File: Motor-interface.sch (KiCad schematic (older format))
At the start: 40 parts, among them J101 0, J102 0, K101 RELAY_2RT, P101 TE-23pins connector, P102 PSU_ISO, P103 Halls, P104 LineContactor, P105 ReverseContactor, P106 FanContactor, P107 Battery+, P108 MC_USB, P109 MC_CAN, Q101 Q_NPN_BCE, U101 AP1117D50, U102 AP1117D33, U103 TLP2361, U104 TLP2361, U105 TLP2361, U106 TLP2361, U107 TLP2361, U108 TLP2361, U109 Teensy_3.2, U110 TLP2361

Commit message: PBC layout
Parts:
- U109: footprint Housings_SSOP:TSSOP-32_6.1x11mm_Pitch0.65mm -> electric_car_lib:Teensy3.2_inv
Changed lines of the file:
@@
 F 0 "U109" H 8000 1750 39  0000 C CNN
 F 1 "Teensy_3.2" H 8000 2450 39  0000 C CNN
-F 2 "Housings_SSOP:TSSOP-32_6.1x11mm_Pitch0.65mm" H 7700 1450 39  0001 C CNN
+F 2 "electric_car_lib:Teensy3.2_inv" H 7700 1450 39  0001 C CNN
 F 3 "" H 7700 1450 39  0000 C CNN
 	1    8000 1900
@@
 	8350 5000 8350 5050
 Wire Wire Line
-	8350 5450 8350 5550
+	8350 5450 8350 5500
+Wire Wire Line
+	8350 5500 8350 5550
 Wire Wire Line
 	8600 5400 8600 5500
@@
 	8600 5000 8600 5100
 Wire Wire Line
-	7600 5000 8600 5000
+	7600 5000 8350 5000
+Wire Wire Line
+	8350 5000 8600 5000
 Connection ~ 8350 5000
 Wire Wire Line
@@
 Hall_Power
 Wire Wire Line
-	4250 3700 4550 3700
+	4250 3700 4450 3700
+Wire Wire Line
+	4450 3700 4550 3700
 Wire Wire Line
 	4850 3700 4950 3700
@@
 	4950 4700 4850 4700
 Wire Wire Line
-	4450 3700 4450 4700
+	4450 3700 4450 4200
+Wire Wire Line
+	4450 4200 4450 4700
 Wire Wire Line
 	4450 4700 4550 4700

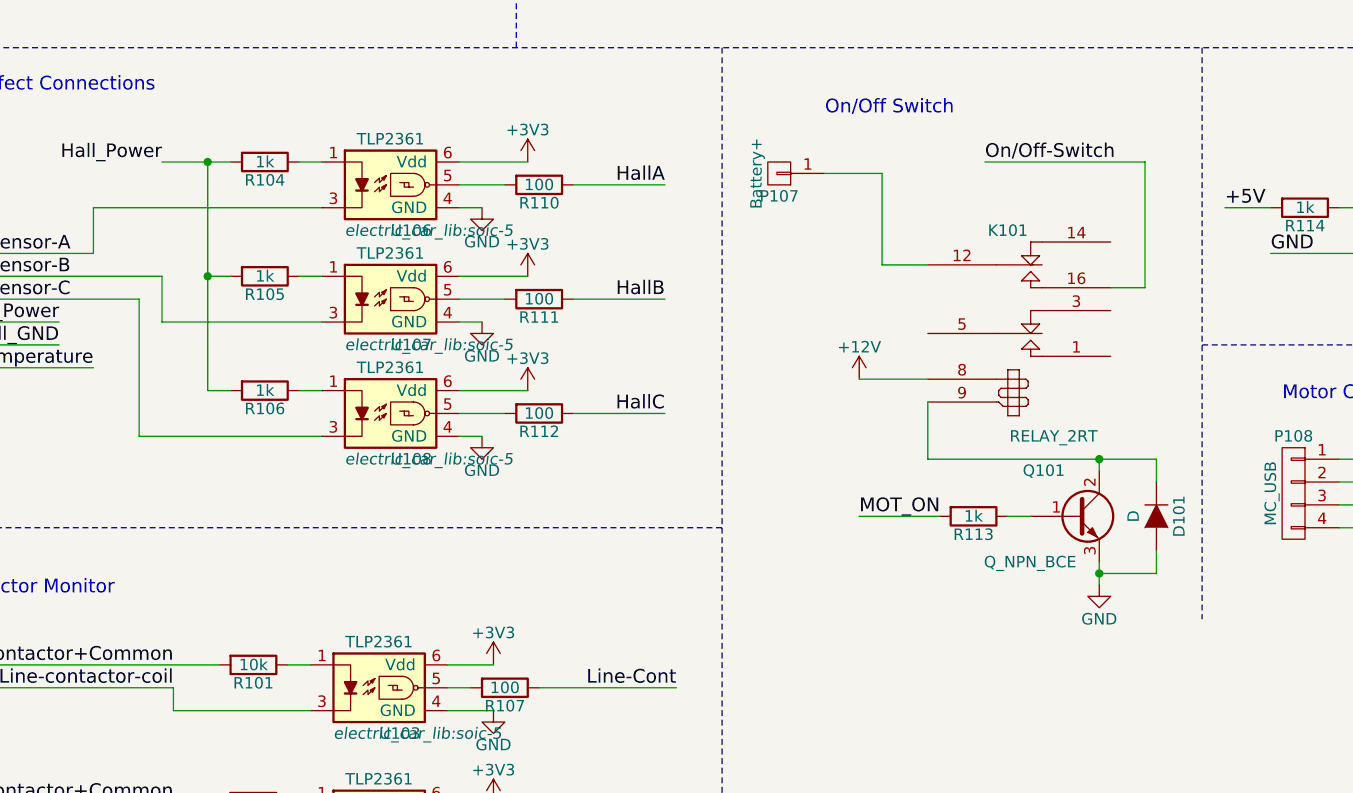
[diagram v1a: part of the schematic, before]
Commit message: changed optos, removed relay, needs ssr
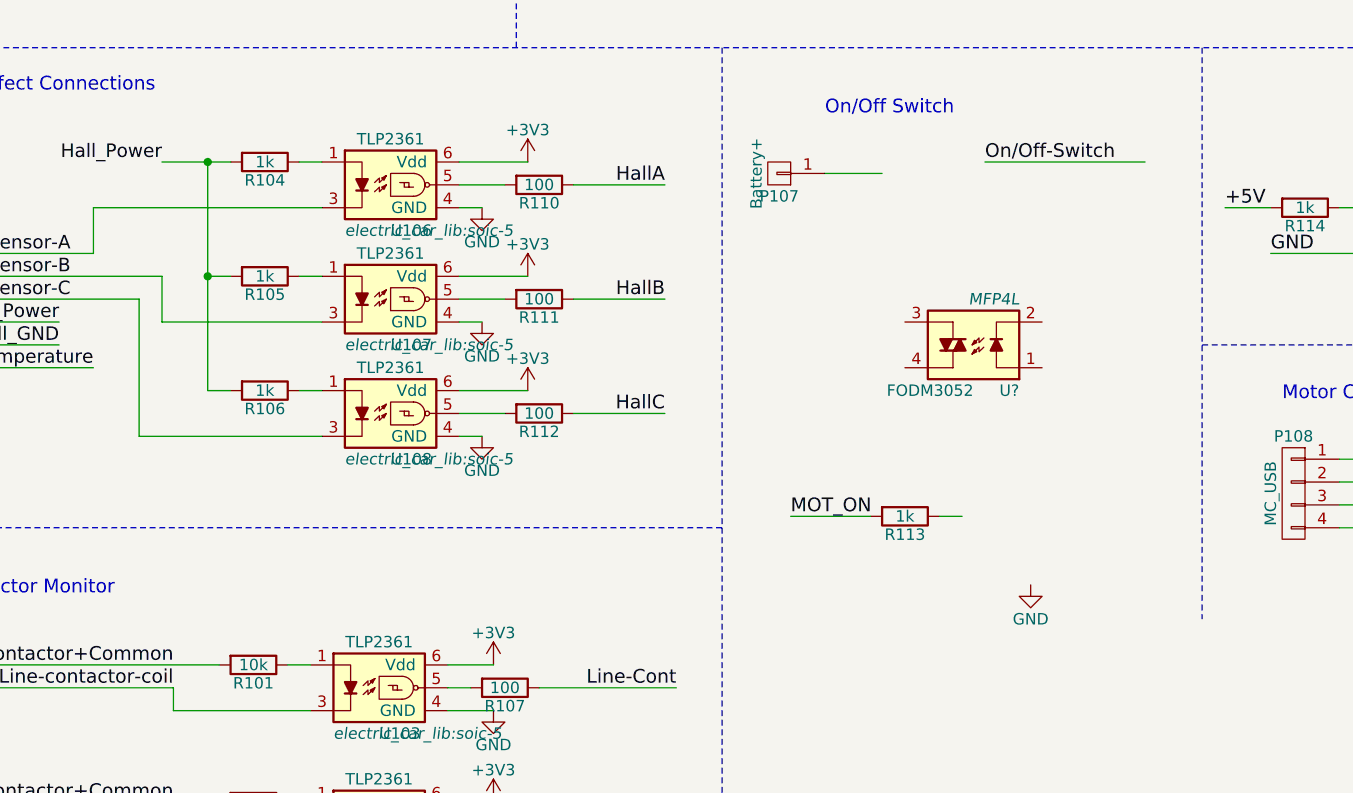
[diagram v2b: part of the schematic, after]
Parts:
- removed D101: D, Diodes_SMD:DO-214AB_Handsoldering, symbol D
- removed K101: RELAY_2RT, Relays_ThroughHole:Relay_SANYOU_SRD_Series_Form_C, symbol RELAY_2RT
- removed Q101: Q_NPN_BCE, TO_SOT_Packages_SMD:SOT-23, symbol Q_NPN_BCE
- added U?: FODM3052, MFP4L, symbol FODM3052
- U101, U102: footprint TO_SOT_Packages_SMD:TO-252-2Lead -> TO_SOT_Packages_SMD:SOT-223
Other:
- moved on the sheet: R113
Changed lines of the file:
@@
 MOSI
-$Comp
-L RELAY_2RT K101
-U 1 1 57FCBA72
-P 8000 4400
-F 0 "K101" H 7950 4800 50  0000 C CNN
-F 1 "RELAY_2RT" H 8150 3900 50  0000 C CNN
-F 2 "Relays_ThroughHole:Relay_SANYOU_SRD_Series_Form_C" H 8000 4400 50  0001 C CNN
-F 3 "" H 8000 4400 50  0000 C CNN
-	1    8000 4400
-	1    0    0    -1
-$EndComp
-$Comp
-L Q_NPN_BCE Q101
-U 1 1 57FCBE60
-P 8250 5250
-F 0 "Q101" H 8200 5450 50  0000 R CNN
-F 1 "Q_NPN_BCE" H 8250 5050 50  0000 R CNN
-F 2 "TO_SOT_Packages_SMD:SOT-23" H 8450 5350 50  0001 C CNN
-F 3 "" H 8250 5250 50  0000 C CNN
-	1    8250 5250
-	1    0    0    -1
-$EndComp
-$Comp
-L +12V #PWR01
-U 1 1 57FCC08A
-P 7300 4650
-F 0 "#PWR01" H 7300 4500 50  0001 C CNN
-F 1 "+12V" H 7300 4790 50  0000 C CNN
-F 2 "" H 7300 4650 50  0000 C CNN
-F 3 "" H 7300 4650 50  0000 C CNN
-	1    7300 4650
-	-1   0    0    -1
-$EndComp
 $Comp
 L GND #PWR02
 U 1 1 57FCC1C9
-P 8350 5550
-F 0 "#PWR02" H 8350 5300 50  0001 C CNN
-F 1 "GND" H 8350 5400 50  0000 C CNN
-F 2 "" H 8350 5550 50  0000 C CNN
-F 3 "" H 8350 5550 50  0000 C CNN
-	1    8350 5550
-	1    0    0    -1
-$EndComp
-Text Label 7300 5250 0    60   ~ 0
+P 8050 5550
+F 0 "#PWR02" H 8050 5300 50  0001 C CNN
+F 1 "GND" H 8050 5400 50  0000 C CNN
+F 2 "" H 8050 5550 50  0000 C CNN
+F 3 "" H 8050 5550 50  0000 C CNN
+	1    8050 5550
+	1    0    0    -1
+$EndComp
+Text Label 7000 5250 0    60   ~ 0
 MOT_ON
 Text Label 9200 2200 2    60   ~ 0
@@
 L R R113
 U 1 1 581878E6
-P 7800 5250
-F 0 "R113" V 7880 5250 50  0000 C CNN
-F 1 "1k" V 7800 5250 50  0000 C CNN
-F 2 "Resistors_SMD:R_1206_HandSoldering" V 7730 5250 50  0001 C CNN
-F 3 "" H 7800 5250 50  0000 C CNN
-	1    7800 5250
+P 7500 5250
+F 0 "R113" V 7580 5250 50  0000 C CNN
+F 1 "1k" V 7500 5250 50  0000 C CNN
+F 2 "Resistors_SMD:R_1206_HandSoldering" V 7430 5250 50  0001 C CNN
+F 3 "" H 7500 5250 50  0000 C CNN
+	1    7500 5250
 	0    1    1    0
 $EndComp
@@
 	1    8850 1200
 	1    0    0    -1
-$EndComp
-$Comp
-L D D101
-U 1 1 582A630A
-P 8600 5250
-F 0 "D101" H 8600 5350 50  0000 C CNN
-F 1 "D" H 8600 5150 50  0000 C CNN
-F 2 "Diodes_SMD:DO-214AB_Handsoldering" H 8600 5250 50  0001 C CNN
-F 3 "" H 8600 5250 50  0000 C CNN
-	1    8600 5250
-	0    1    1    0
 $EndComp
 $Comp
@@
 Wire Wire Line
 	8700 2500 8900 2500
-Wire Wire Line
-	7300 4650 7600 4650
-Wire Wire Line
-	8550 4250 8400 4250
 Wire Notes Line
 	700  3200 10750 3200
@@
 	7150 3750 7400 3750
 Wire Wire Line
-	7400 3750 7400 4150
-Wire Wire Line
-	7400 4150 7600 4150
-Wire Wire Line
 	3200 5900 4500 5900
 Wire Wire Line
@@
 	3200 6600 4300 6600
 Wire Wire Line
-	7950 5250 8050 5250
-Wire Wire Line
-	7650 5250 7300 5250
+	7650 5250 7750 5250
+Wire Wire Line
+	7350 5250 7000 5250
 Wire Notes Line
 	2600 600  2600 7150
@@
 Wire Wire Line
 	8700 1200 8850 1200
-Wire Wire Line
-	8350 5000 8350 5050
-Wire Wire Line
-	8350 5450 8350 5500
-Wire Wire Line
-	8350 5500 8350 5550
-Wire Wire Line
-	8600 5400 8600 5500
-Wire Wire Line
-	8600 5500 8350 5500
-Connection ~ 8350 5500
-Wire Wire Line
-	8600 5000 8600 5100
-Wire Wire Line
-	7600 5000 8350 5000
-Wire Wire Line
-	8350 5000 8600 5000
-Connection ~ 8350 5000
 Wire Wire Line
 	6200 1500 7300 1500
@@
 Hall_Power
 Wire Wire Line
-	4250 3700 4450 3700
-Wire Wire Line
-	4450 3700 4550 3700
+	4250 3700 4550 3700
 Wire Wire Line
 	4850 3700 4950 3700
@@
 	4950 4700 4850 4700
 Wire Wire Line
-	4450 3700 4450 4200
-Wire Wire Line
-	4450 4200 4450 4700
+	4450 3700 4450 4700
 Wire Wire Line
 	4450 4700 4550 4700
@@
 F 0 "U102" H 2100 2050 50  0000 C CNN
 F 1 "AP1117D33" H 2000 2550 50  0000 C CNN
-F 2 "TO_SOT_Packages_SMD:TO-252-2Lead" H 2000 2300 50  0001 C CNN
+F 2 "TO_SOT_Packages_SMD:SOT-223" H 2000 2300 50  0001 C CNN
 F 3 "" H 2000 2300 50  0000 C CNN
 	1    2000 2300
@@
 F 0 "U101" H 1100 950 50  0000 C CNN
 F 1 "AP1117D50" H 1000 1450 50  0000 C CNN
-F 2 "TO_SOT_Packages_SMD:TO-252-2Lead" H 1000 1200 50  0001 C CNN
+F 2 "TO_SOT_Packages_SMD:SOT-223" H 1000 1200 50  0001 C CNN
 F 3 "" H 1000 1200 50  0000 C CNN
 	1    1000 1200
@@
 Wire Notes Line
 	8800 4500 11100 4500
-Wire Wire Line
-	8550 3700 8550 4250
 Wire Wire Line
 	2000 2700 2000 2600
@@
 Wire Wire Line
 	1700 1350 1900 1350
-Wire Wire Line
-	7600 5000 7600 4750
 $Comp
 L C C101
@@
 Wire Notes Line
 	2600 5300 6700 5300
+$Comp
+L FODM3052 U?
+U 1 1 582C070F
+P 7800 4500
+F 0 "U?" H 7600 4700 50  0000 L CNN
+F 1 "FODM3052" H 7800 4700 50  0000 L CNN
+F 2 "MFP4L" H 7600 4300 50  0000 L CIN
+F 3 "" H 7775 4500 50  0000 L CNN
+	1    7800 4500
+	-1   0    0    1
+$EndComp
 $EndSCHEMATC

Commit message: minor tweaks, started layout
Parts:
- removed P107: Battery+, symbol CONN_01X01
- added P107: Battery+, Connect:bornier2, symbol CONN_01X02
- added Q101: Q_NPN_BCE, TO_SOT_Packages_SMD:SOT-428, symbol Q_NPN_BCE
- C101: value C -> 10uF
- U111: renamed from U?; footprint MFP4L -> electric_car_lib:MFP4L
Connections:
- net GND: now also U111.2
- net On/Off-Switch: now also U111.3, Q101.3 (E)
- net at R113.1: now also U111.1
- net at U111.4: now also Q101.1 (B)
- new net: P107.1 (P1), P107.2 (P2), Q101.2 (C)
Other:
- moved on the sheet: R113, U111

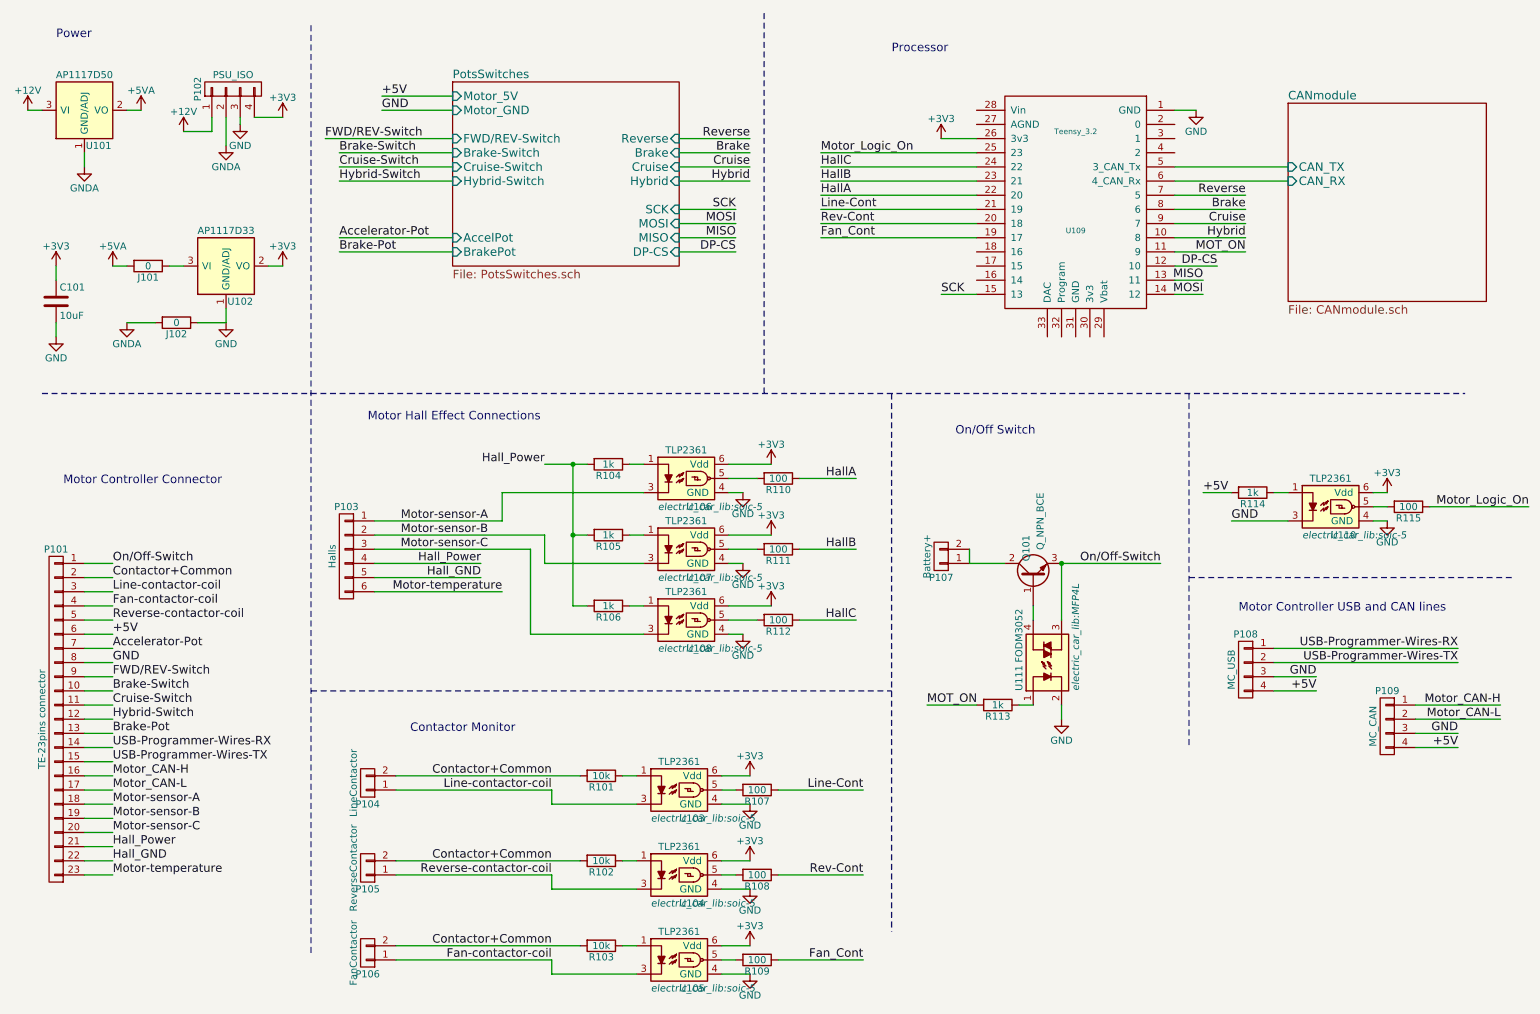
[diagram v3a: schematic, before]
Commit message: swapped pins, arranged parts
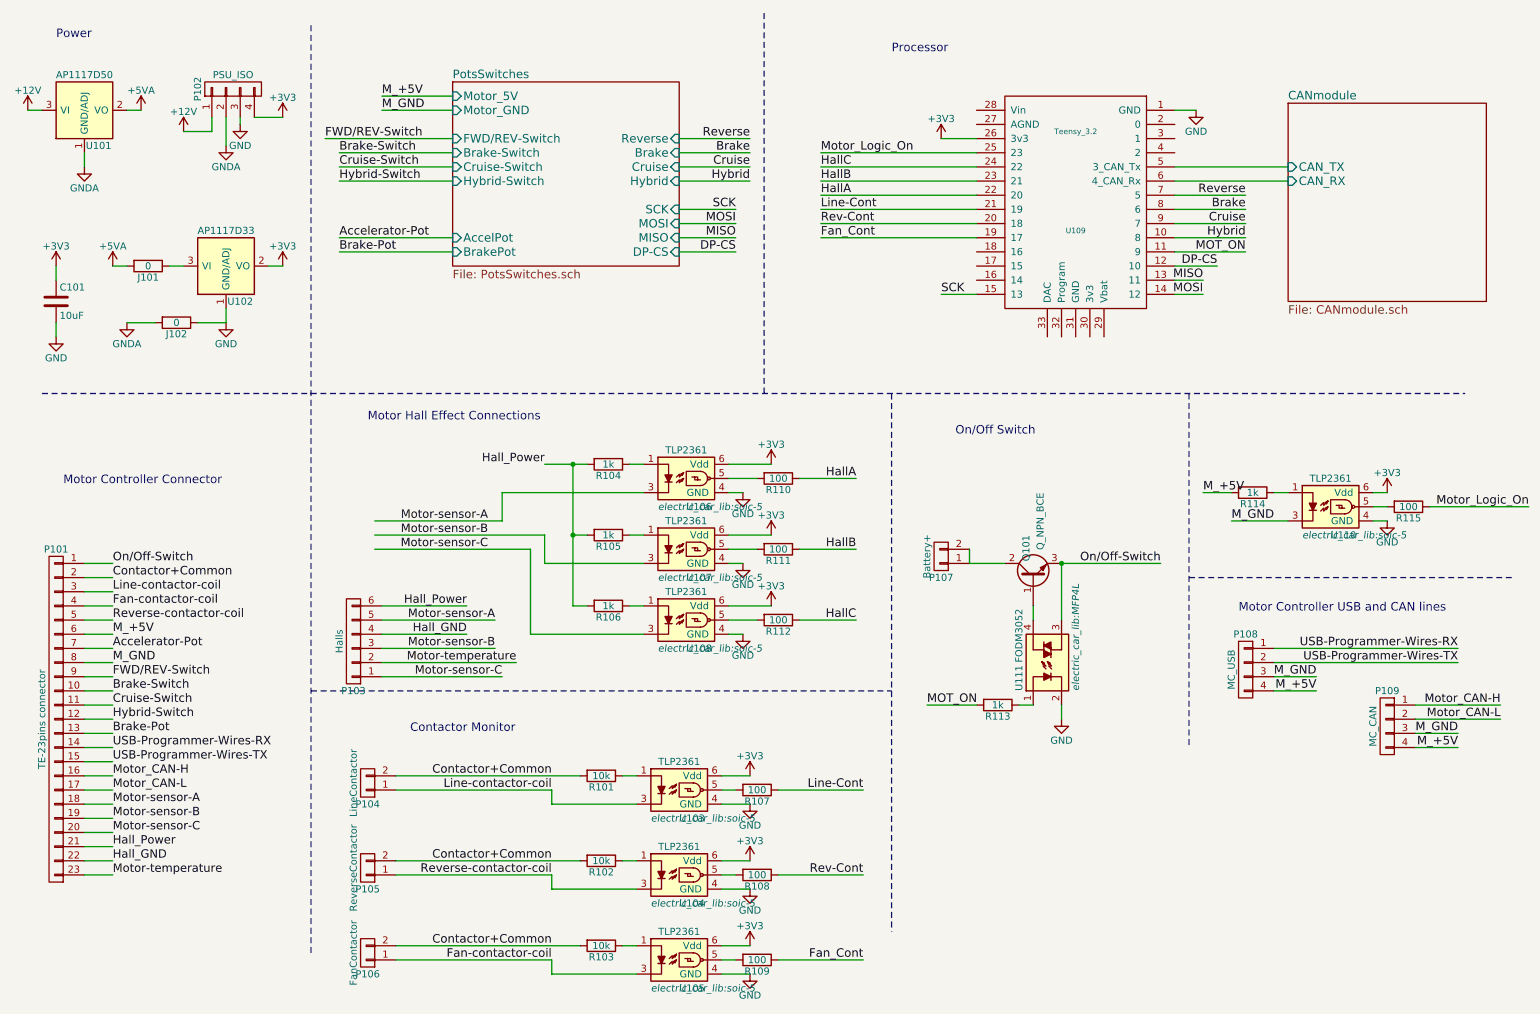
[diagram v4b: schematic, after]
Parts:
- P103: footprint Pin_Headers:Pin_Header_Straight_1x06 -> Pin_Headers:Pin_Header_Angled_2x03
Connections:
- net GND: no longer P101.8 (P8), P108.3 (P3), P109.3 (P3), U110.3
- net Hall_GND: now also P103.4 (P4); no longer P103.5 (P5)
- net Hall_Power: now also P103.6 (P6); no longer P103.4 (P4)
- net Motor-sensor-A: now also P103.5 (P5); no longer P103.1 (P1)
- net Motor-sensor-B: now also P103.3 (P3); no longer P103.2 (P2)
- net Motor-sensor-C: now also P103.1 (P1); no longer P103.3 (P3)
- net Motor-temperature: now also P103.2 (P2); no longer P103.6 (P6)
- net +5V renamed M_+5V
- new net M_GND: P101.8 (P8), P108.3 (P3), P109.3 (P3), U110.3
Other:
- moved on the sheet: P103
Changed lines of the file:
@@
 Reverse-contactor-coil
 Text Label 1200 4900 0    60   ~ 0
-+5V
+M_+5V
 Text Label 1200 5000 0    60   ~ 0
 Accelerator-Pot
 Text Label 1200 5100 0    60   ~ 0
-GND
+M_GND
 Text Label 1200 5200 0    60   ~ 0
 FWD/REV-Switch
@@
 L CONN_01X06 P103
 U 1 1 5821DB26
-P 2850 4350
-F 0 "P103" H 2850 4700 50  0000 C CNN
-F 1 "Halls" V 2950 4350 50  0000 C CNN
-F 2 "Pin_Headers:Pin_Header_Straight_1x06" H 2850 4350 50  0001 C CNN
-F 3 "" H 2850 4350 50  0000 C CNN
-	1    2850 4350
-	-1   0    0    -1
+P 2900 4950
+F 0 "P103" H 2900 5300 50  0000 C CNN
+F 1 "Halls" V 3000 4950 50  0000 C CNN
+F 2 "Pin_Headers:Pin_Header_Angled_2x03" H 2900 4950 50  0001 C CNN
+F 3 "" H 2900 4950 50  0000 C CNN
+	1    2900 4950
+	-1   0    0    1
 $EndComp
 Text Label 3850 4100 2    59   ~ 0
@@
 Text Label 1200 6600 0    59   ~ 0
 Motor-temperature
-Text Label 3950 4600 2    59   ~ 0
+Text Label 4050 5100 2    59   ~ 0
 Motor-temperature
 $Comp
@@
 Brake-Pot
 Text Label 3100 1100 0    60   ~ 0
-+5V
+M_+5V
 Text Label 3100 1200 0    60   ~ 0
-GND
+M_GND
 $Comp
 L R R101
@@
 Fan_Cont
 Text Label 9700 5200 2    60   ~ 0
-GND
+M_GND
 Text Label 9700 5300 2    60   ~ 0
-+5V
+M_+5V
 Text Label 10700 5600 2    60   ~ 0
-GND
-Text Label 3800 4400 2    59   ~ 0
+M_GND
+Text Label 3700 4700 2    59   ~ 0
 Hall_Power
 Text Label 10700 5700 2    60   ~ 0
-+5V
-Text Label 3800 4500 2    59   ~ 0
+M_+5V
+Text Label 3700 4900 2    59   ~ 0
 Hall_GND
 Text Label 1200 6200 0    59   ~ 0
@@
 	6200 2100 7300 2100
 Wire Wire Line
-	3950 4600 3050 4600
-Wire Wire Line
-	3050 4500 3800 4500
-Wire Wire Line
 	3050 4300 4150 4300
 Wire Wire Line
@@
 Wire Wire Line
 	3050 4100 3950 4100
-Wire Wire Line
-	3800 4400 3050 4400
 Wire Wire Line
 	10700 5000 9400 5000
@@
 $EndComp
 Text Label 8900 3900 0    60   ~ 0
-+5V
+M_+5V
 Text Label 9100 4100 0    60   ~ 0
-GND
+M_GND
 Wire Wire Line
 	9500 4100 9100 4100
@@
 Wire Wire Line
 	7250 4300 7250 4400
+Text Label 3900 4800 2    59   ~ 0
+Motor-sensor-A
+Text Label 3900 5000 2    59   ~ 0
+Motor-sensor-B
+Text Label 3950 5200 2    59   ~ 0
+Motor-sensor-C
+Wire Wire Line
+	3700 4700 3100 4700
+Wire Wire Line
+	3100 4800 3900 4800
+Wire Wire Line
+	3700 4900 3100 4900
+Wire Wire Line
+	3100 5000 3900 5000
+Wire Wire Line
+	4050 5100 3100 5100
+Wire Wire Line
+	3100 5200 3950 5200
 $EndSCHEMATC

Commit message: laid out halls and pots
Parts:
- U109: footprint electric_car_lib:Teensy3.2_inv -> electric_car_lib:Teensy3.2
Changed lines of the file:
@@
 F 0 "U109" H 8000 1750 39  0000 C CNN
 F 1 "Teensy_3.2" H 8000 2450 39  0000 C CNN
-F 2 "electric_car_lib:Teensy3.2_inv" H 7700 1450 39  0001 C CNN
+F 2 "electric_car_lib:Teensy3.2" H 7700 1450 39  0001 C CNN
 F 3 "" H 7700 1450 39  0000 C CNN
 	1    8000 1900
